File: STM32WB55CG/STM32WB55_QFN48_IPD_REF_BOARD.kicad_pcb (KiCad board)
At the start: 2 copper layers, 17 parts, among them IC1 LD3985M33R, IC2 USBLC6-2SC6, J1 USB_B_Micro, U1 MCP1640CCH, U2 STM32WB55CG, U3 MLL1200S TE, U4 BNO055_my, U5 ADS1115IDGS, Y1 NX2520SA-32MHz, Y2 NX2012SA-32768K, Y3 NX2012SA-32768K

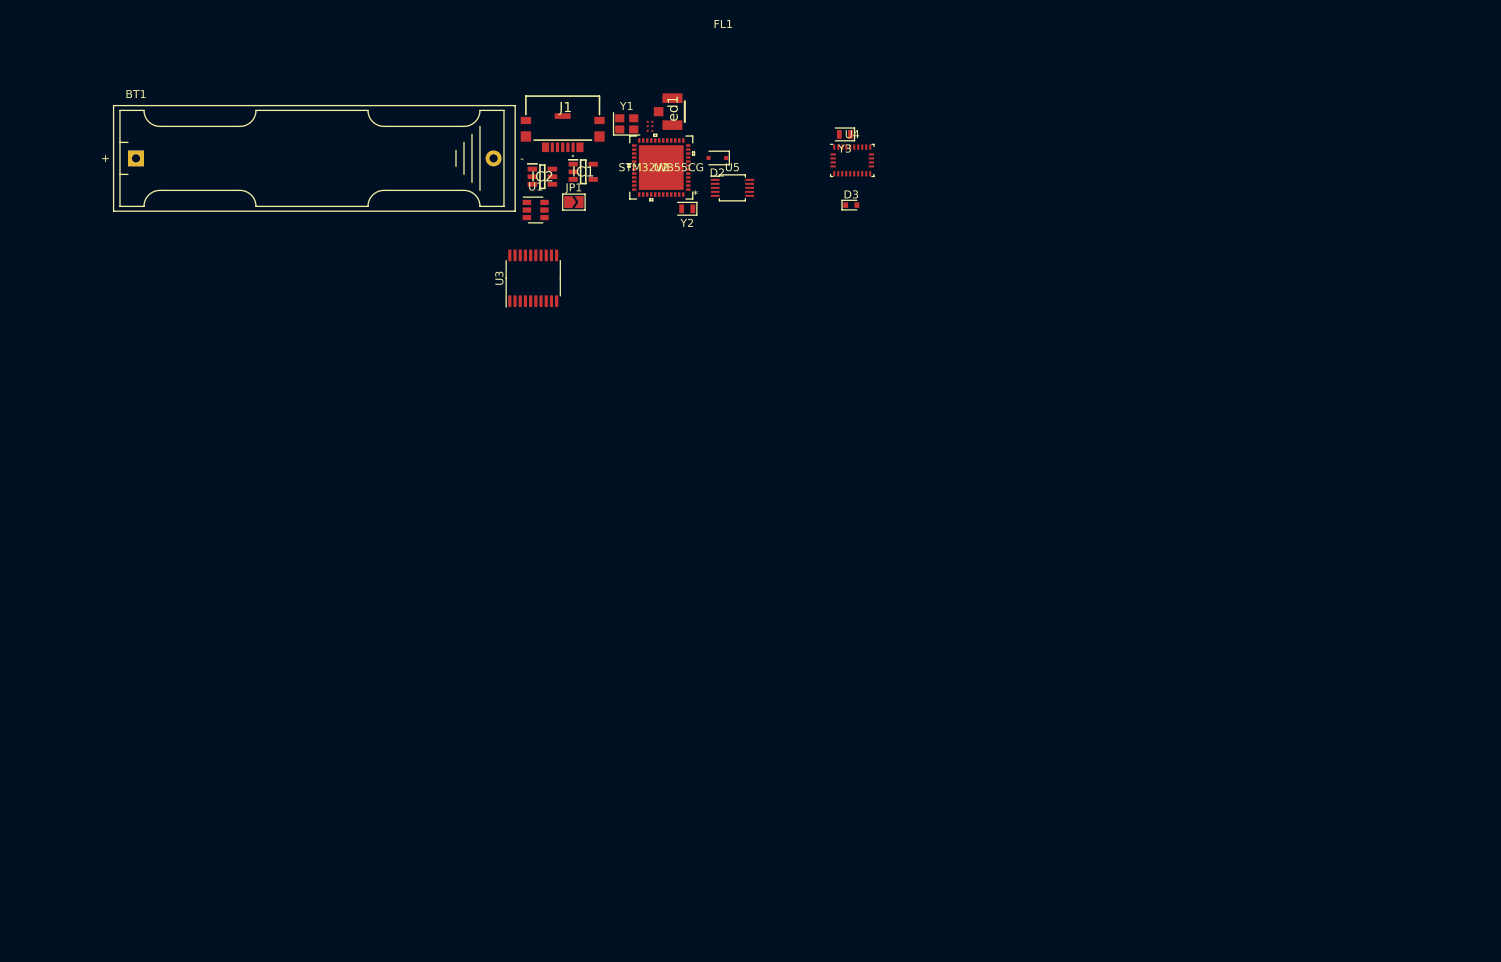
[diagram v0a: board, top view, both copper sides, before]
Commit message: assign footprints complete need one more look and a check from Simek
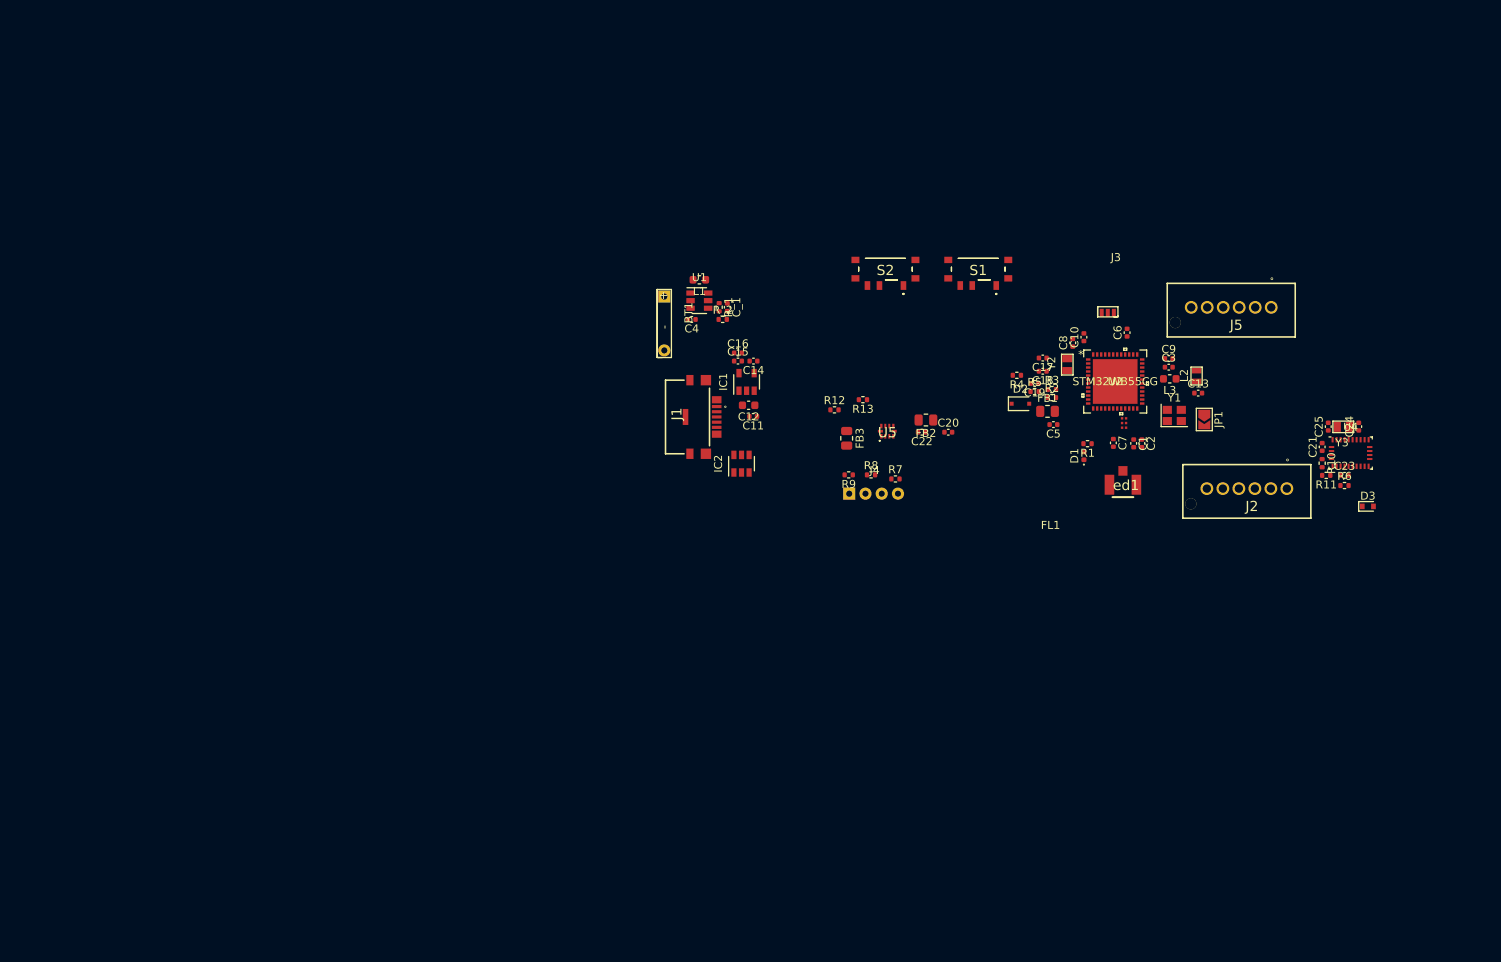
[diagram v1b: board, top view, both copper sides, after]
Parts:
- removed U3: MLL1200S TE, Package_SO:TSSOP-20_4.4x6.5mm_P0.65mm
- added C1: 100n, Capacitor_SMD:C_0402_1005Metric, F.Cu at (212.0, 94.3)
- added C10: 100n, Capacitor_SMD:C_0402_1005Metric, F.Cu at (205.7, 81.0)
- added C11: 1u, Capacitor_SMD:C_0402_1005Metric, F.Cu at (164.4, 90.9)
- added C12: 100n, Capacitor_SMD:C_0603_1608Metric, F.Cu at (163.8, 89.5)
- added C13: 4u7, Capacitor_SMD:C_0402_1005Metric, F.Cu at (220.0, 88.0)
- added C14: 10n, Capacitor_SMD:C_0402_1005Metric, F.Cu at (164.4, 84.0)
- added C15: 100n, Capacitor_SMD:C_0402_1005Metric, F.Cu at (162.5, 84.0)
- added C16: 1u, Capacitor_SMD:C_0402_1005Metric, F.Cu at (162.5, 83.0)
- added C17: 4p3, Capacitor_SMD:C_0402_1005Metric, F.Cu at (200.6, 83.6)
- added C18: 4p3, Capacitor_SMD:C_0402_1005Metric, F.Cu at (200.6, 85.3)
- added C19: 100n, Capacitor_SMD:C_0402_1005Metric, F.Cu at (199.6, 86.8)
- added C2: 100p, Capacitor_SMD:C_0402_1005Metric, F.Cu at (213.0, 94.3)
- added C20: 1u, Capacitor_SMD:C_0402_1005Metric, F.Cu at (188.8, 92.9)
- added C21: 100n, Capacitor_SMD:C_0402_1005Metric, F.Cu at (235.5, 94.7)
- added C22: 1u, Capacitor_SMD:C_0402_1005Metric, F.Cu at (185.5, 92.9)
- added C23: 1u, Capacitor_SMD:C_0402_1005Metric, F.Cu at (238.3, 98.3)
- added C24: 22p, Capacitor_SMD:C_0402_1005Metric, F.Cu at (240.1, 92.2)
- added C25: 22p, Capacitor_SMD:C_0402_1005Metric, F.Cu at (236.3, 92.2)
- added C3: 4u7, Capacitor_SMD:C_0402_1005Metric, F.Cu at (216.3, 84.8)
- added C4: 4u7, Capacitor_SMD:C_0402_1005Metric, F.Cu at (156.7, 78.8)
- added C5: 100n, Capacitor_SMD:C_0402_1005Metric, F.Cu at (201.9, 91.9)
- added C6: 100n, Capacitor_SMD:C_0402_1005Metric, F.Cu at (211.1, 80.5)
- added C7: 100n, Capacitor_SMD:C_0402_1005Metric, F.Cu at (209.4, 94.2)
- added C8: 100n, Capacitor_SMD:C_0402_1005Metric, F.Cu at (204.3, 81.7)
- added C9: 100n, Capacitor_SMD:C_0402_1005Metric, F.Cu at (216.3, 83.7)
- added C_1: 10u, Capacitor_SMD:C_0402_1005Metric, F.Cu at (161.2, 77.3)
- added D1: LED Blue, LED_SMD:LED_0402_1005Metric, F.Cu at (205.7, 95.9)
- added FB1: Z0805C601BSMST, Resistor_SMD:R_0805_2012Metric, F.Cu at (201.2, 90.3)
- added FB2: MMZ2012Y152BTD25, Resistor_SMD:R_0805_2012Metric, F.Cu at (186.0, 91.4)
- added FB3: MMZ2012Y152BTD25, Resistor_SMD:R_0805_2012Metric, F.Cu at (176.1, 93.7)
- added J2: Conn_01x06_Male, Molexkonektor:55932-0610, F.Cu at (226.1, 96.9)
- added J3: Conn_01x03_Male, 0Pretty:PCB_Pin_connector, F.Cu at (209.7, 77.5)
- added J4: Conn_01x04_Male, 0Pretty:Pin_FSR, F.Cu at (178.6, 99.8)
- added J5: Conn_01x06_Male, Molexkonektor:55932-0610, F.Cu at (224.2, 74.3)
- added L1: 4u7, Inductor_SMD:L_0603_1608Metric, F.Cu at (157.7, 73.9)
- added L2: 10u, 0Pretty:L_0712_SMD, F.Cu at (219.8, 85.9)
- added L3: 10n, Inductor_SMD:L_0603_1608Metric, F.Cu at (216.5, 86.2)
- added R1: 100K, Resistor_SMD:R_0402_1005Metric, F.Cu at (206.2, 94.3)
- added R10: 10K, Resistor_SMD:R_0402_1005Metric, F.Cu at (235.5, 96.8)
- added R11: 10K, Resistor_SMD:R_0402_1005Metric, F.Cu at (236.0, 98.3)
- added R12: 10K, Resistor_SMD:R_0402_1005Metric, F.Cu at (174.6, 90.1)
- added R13: 10K, Resistor_SMD:R_0402_1005Metric, F.Cu at (178.1, 88.8)
- added R2: 10K, Resistor_SMD:R_0402_1005Metric, F.Cu at (201.7, 88.6)
- added R3: 10K, Resistor_SMD:R_0402_1005Metric, F.Cu at (201.7, 87.6)
- added R4: 10K, Resistor_SMD:R_0402_1005Metric, F.Cu at (197.4, 85.8)
- added R5: 100K, Resistor_SMD:R_0402_1005Metric, F.Cu at (199.6, 87.8)
- added R6: 10K, Resistor_SMD:R_0402_1005Metric, F.Cu at (238.3, 99.6)
- added R7: 100K, Resistor_SMD:R_0402_1005Metric, F.Cu at (182.2, 98.7)
- added R8: 100K, Resistor_SMD:R_0402_1005Metric, F.Cu at (179.1, 98.2)
- added R9: 100K, Resistor_SMD:R_0402_1005Metric, F.Cu at (176.3, 98.2)
- added R_1: 976k, Resistor_SMD:R_0402_1005Metric, F.Cu at (160.1, 77.3)
- added R_2: 562k, Resistor_SMD:R_0402_1005Metric, F.Cu at (160.6, 78.8)
- added S1: MLL1200S, vypinac:MLL1200S, F.Cu at (192.5, 72.5)
- added S2: MLL1200S, vypinac:MLL1200S, F.Cu at (180.9, 72.5)
- BT1: footprint Battery:BatteryHolder_Keystone_2466_1xAAA -> 0Pretty:battery_connector
- IC1: footprint USBRegulator:SOT95P280X145-5N -> Package_TO_SOT_SMD:SOT-23-5
- IC2: footprint USB_data:SOT95P280X145-6N -> Package_TO_SOT_SMD:SOT-23-6
- U5: footprint Package_SO:TSSOP-10_3x3mm_P0.5mm -> ADS1115:ADS1115IRUGR
- Y2, Y3: footprint Crystal:Crystal_SMD_2012-2Pin_2.0x1.2mm -> 0Pretty:Crystal_2012_custom
- moved JP1 83.4 mm to (220.8, 91.3), turned to 270 degrees
- moved Y1 77.6 mm to (217.0, 90.8)
- moved D3 74.8 mm to (241.2, 102.2)
- moved ed1 73.1 mm to (210.6, 99.5), turned to 180 degrees
- moved U4 72.2 mm to (239.1, 95.5)
- moved Y3 72.2 mm to (238.2, 92.3)
- moved FL1 71.6 mm to (211.2, 92.6), turned to 180 degrees
- moved BT1 69.7 mm to (154.2, 78.1), turned to 270 degrees
- moved U2 62.7 mm to (209.7, 86.6), turned to 0 degrees
- moved Y2 51.3 mm to (203.6, 84.5), turned to 90 degrees
- moved D2 48.8 mm to (197.8, 89.3), turned to 0 degrees
- moved IC2 43.7 mm to (162.9, 96.8), turned to 90 degrees
- moved J1 39.2 mm to (158.9, 91.0), turned to 270 degrees
- moved U5 36.1 mm to (181.2, 92.8)
- moved IC1 33.3 mm to (163.6, 86.6), turned to 90 degrees
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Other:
- copper layers 2 -> 4

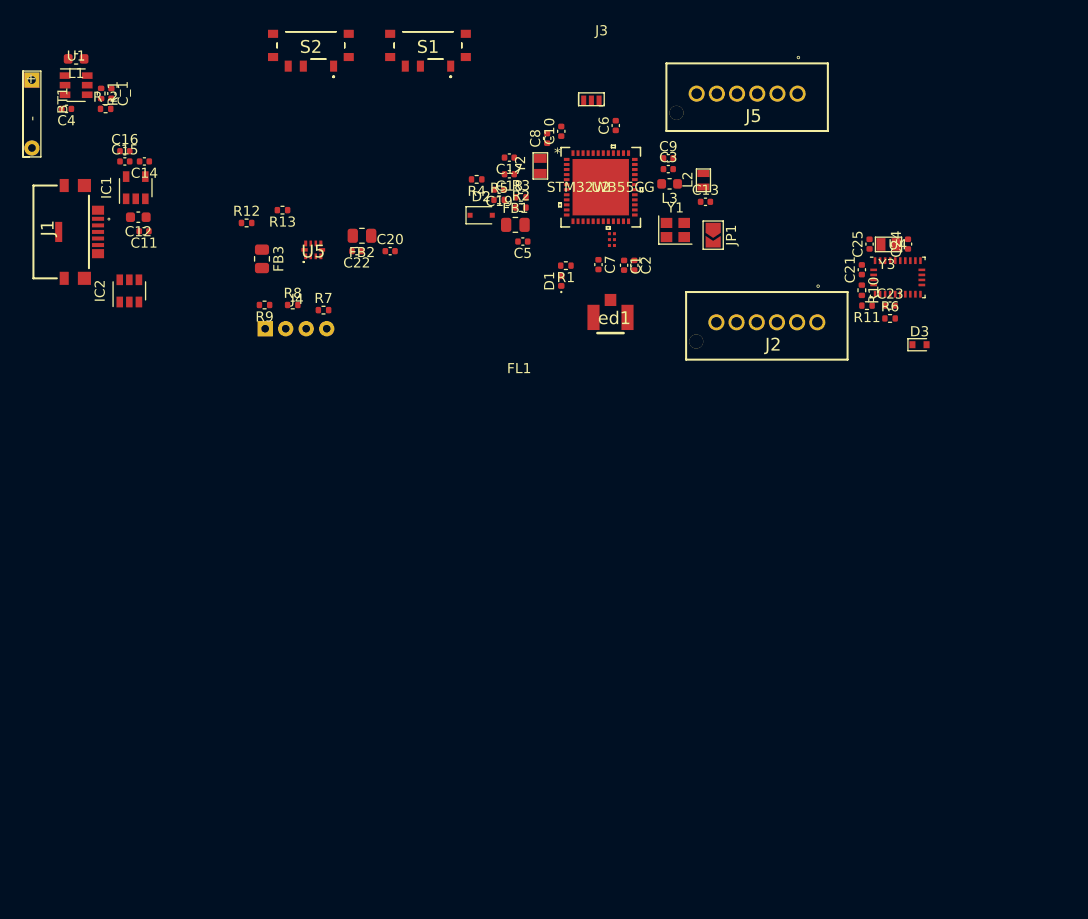
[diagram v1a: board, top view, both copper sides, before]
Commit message: dokoncene rozlozenie okolo STM32WB podla referencneho dizajnu
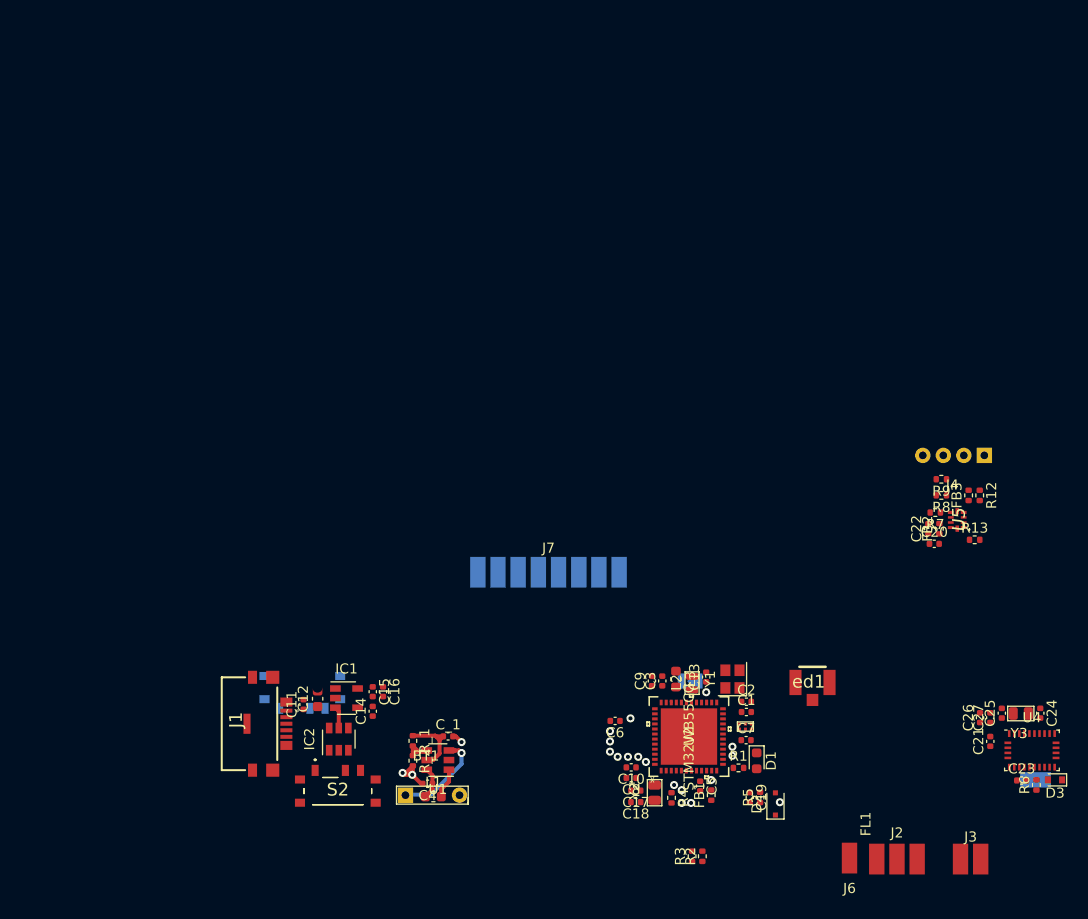
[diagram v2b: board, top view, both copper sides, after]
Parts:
- removed R10, R11: 10K, Resistor_SMD:R_0402_1005Metric
- added C26: 100n, Capacitor_SMD:C_0402_1005Metric, F.Cu at (247.2, 139.1)
- added C27: 100n, Capacitor_SMD:C_0402_1005Metric, F.Cu at (248.2, 139.1)
- added J6: Conn_01x01_Male, 0Pretty:pin_01, F.Cu at (234.3, 153.0)
- added J7: Conn_01x08_Male, 0Pretty:pin_08, F.Cu at (204.5, 124.7)
- BT1: footprint 0Pretty:battery_connector -> 0Pretty:battery_connector_narrow
- C23: value 1u -> 100n
- D1: footprint LED_SMD:LED_0402_1005Metric -> LED_SMD:LED_0603_1608Metric
- FB1: value Z0805C601BSMST -> BLM15AX601SN1D; footprint Resistor_SMD:R_0805_2012Metric -> Resistor_SMD:R_0402_1005Metric
- FB2, FB3: footprint Resistor_SMD:R_0805_2012Metric -> Resistor_SMD:R_0402_1005Metric
- J2: value Conn_01x06_Male -> Conn_01x05_Male; footprint Molexkonektor:55932-0610 -> 0Pretty:pin_03
- J3: value Conn_01x03_Male -> Conn_01x02_Male; footprint 0Pretty:PCB_Pin_connector -> 0Pretty:pin_02
- J5: value Conn_01x06_Male -> Conn_01x01_Male; footprint Molexkonektor:55932-0610 -> 0Pretty:pin_01; moved to B.Cu
- JP1, S1: moved to B.Cu
- moved J3 84.0 mm to (246.3, 153.1), turned to 180 degrees
- moved L1 81.2 mm to (193.1, 146.9), turned to 0 degrees
- moved BT1 77.9 mm to (192.5, 145.9), turned to 0 degrees
- moved R12 77.5 mm to (247.2, 117.1), turned to 270 degrees
- moved J5 76.5 mm to (252.7, 145.3), turned to 270 degrees
- moved R13 76.0 mm to (246.7, 121.5), turned to 0 degrees
- moved U1 75.9 mm to (193.5, 143.3), turned to 180 degrees
- moved C4 75.8 mm to (192.5, 145.7)
- moved S2 73.9 mm to (183.6, 146.4), turned to 0 degrees
- moved FB3 73.8 mm to (246.1, 117.1), turned to 90 degrees
- moved C_1 71.9 mm to (194.5, 141.0), turned to 0 degrees
- moved R_2 71.4 mm to (191.0, 143.4), turned to 270 degrees
- moved R_1 71.2 mm to (191.0, 141.4)
- moved R9 69.2 mm to (243.4, 115.5)
- moved U5 69.2 mm to (245.0, 119.5), turned to 90 degrees
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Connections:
- net Net-(IC2-Pad4) renamed USB_OD+
- net Net-(IC2-Pad6) renamed USB_OD-
- J3 pad 1: GENERAL_PIN_OUT3 -> I2C_SCL
- J3 pad 2: GENERAL_PIN_OUT2 -> I2C_SDA
- J5 pad 1: +3V3 -> BNO055_RESET
- U2 pad 14: GENERAL_PIN_OUT1 -> Net-(U2-Pad14)
- U2 pad 42: Net-(U2-Pad42) -> GENERAL_PIN_OUT1
- U2 pad 49: (no net) -> GND
- U4 pad 5: Net-(R10-Pad1) -> GND
- U4 pad 6: Net-(R11-Pad1) -> GND
- Y1 pad 2: Net-(U2-Pad25) -> GND
- Y1 pad 3: GND -> Net-(U2-Pad25)
- Y1 pad 4: (no net) -> GND
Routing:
- net +1V5: track 0.00 -> 12.8 mm, vias 0 -> 1
- net 3v3fromBAT: track 0.00 -> 7.04 mm
- net GND: track 0.00 -> 5.75 mm, vias 0 -> 3
- net Net-(L1-Pad2): track 0.00 -> 3.34 mm
- net Net-(R_1-Pad2): track 0.00 -> 3.10 mm
- net +5V: track 0.00 -> 2.15 mm
- net I2C_SCL: track 0.00 -> 0.06 mm, vias 0 -> 1
- net SYS_JTMS-SWDIO: vias 0 -> 1
- net SYS_JTDO-SWO: vias 0 -> 1
- net SYS_JTCK-SWCLK: vias 0 -> 1
- net SPI_SCK: vias 0 -> 1
- net SPI_MOSI: vias 0 -> 1
- net SPI_MISO: vias 0 -> 1
- net Net-(R4-Pad1): vias 0 -> 1
- net Net-(C19-Pad1): vias 0 -> 2
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
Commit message: in the middle of moving libs
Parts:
- removed S1: MLL1200S, vypinac:MLL1200S
- S2: moved to B.Cu
- moved ed1 117.4 mm to (118.1, 102.1)
- moved C20 116.3 mm to (127.1, 109.1), turned to 270 degrees
- moved R7 116.3 mm to (127.1, 107.1), turned to 270 degrees
- moved J3 115.9 mm to (137.3, 113.6)
- moved J6 115.9 mm to (125.3, 113.5)
- moved J2 115.9 mm to (130.0, 113.6)
- moved C2 115.4 mm to (113.6, 104.4)
- moved C7 115.4 mm to (113.6, 108.2)
- moved R4 115.4 mm to (106.2, 113.9)
- moved C10 115.4 mm to (102.2, 110.9)
- moved C17 115.4 mm to (102.6, 113.2)
- moved C18 115.4 mm to (102.6, 114.3)
- moved D1 115.4 mm to (114.6, 110.3)
- moved JP1 115.4 mm to (108.0, 102.4)
- moved L3 115.4 mm to (106.6, 102.2)
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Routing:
- net GND: track 5.75 -> 105.9 mm, vias 3 -> 31
- net +3V3: track 0.11 -> 36.7 mm, vias 0 -> 13
- net USB_D-: track 0.00 -> 24.3 mm
- net USB_D+: track 0.00 -> 21.5 mm
- net SYS_JTMS-SWDIO: track 0.00 -> 20.8 mm
- net SYS_JTCK-SWCLK: track 0.00 -> 18.5 mm
- net 3v3fromUSB: track 0.00 -> 18.3 mm, vias 0 -> 2
- net Net-(D3-Pad2): track 0.00 -> 16.1 mm
- net GENERAL_PIN_OUT1: track 0.00 -> 15.7 mm
- net SYS_JTDO-SWO: track 0.00 -> 13.4 mm
- net GENERAL_PIN_OUT2: track 0.00 -> 11.1 mm
- net GENERAL_PIN_OUT3: track 0.00 -> 10.2 mm
- net +5V: track 2.15 -> 11.1 mm
- net USB_OD+: track 0.00 -> 7.93 mm
- net Net-(C13-Pad1): track 0.00 -> 5.46 mm
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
